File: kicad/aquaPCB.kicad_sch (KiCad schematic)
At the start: 0 parts

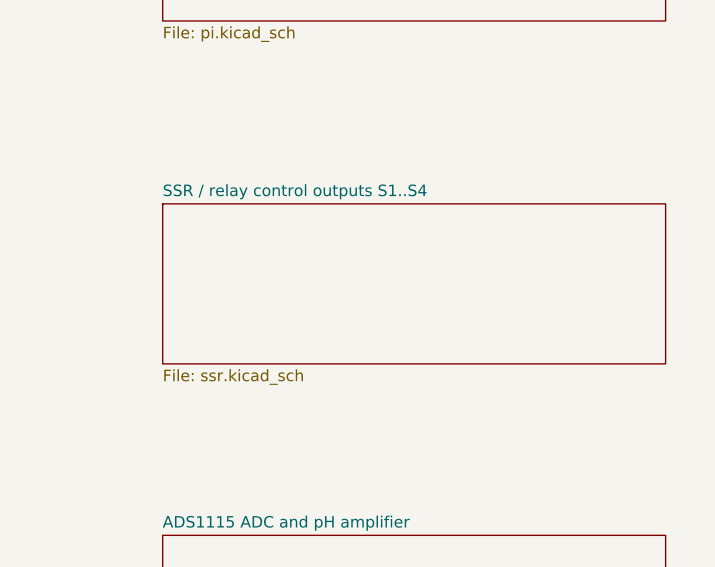
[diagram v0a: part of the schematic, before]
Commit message: kicad: strip obsolete v1 parts for v2 (SSR sheet, IN1..IN4, pH front end)
41 parts, their tracks/vias, pH guard zones, BNC keep-out and port silk removed; freed J2/U5 pins marked no-connect. ERC 0, DRC 0, parity 0; one expected +3V3 ratsnest to J24/JP3/J27/D28 left for the v2 layout.

Co-Authored-By: Claude Opus 5.5 <noreply@anthropic.com>
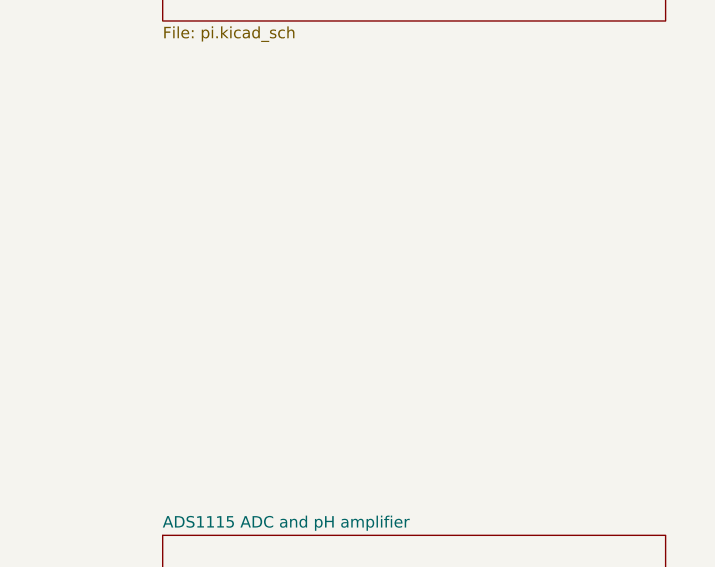
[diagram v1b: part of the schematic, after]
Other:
- removed sheet SSR / relay control outputs S1..S4
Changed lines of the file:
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@@
 			(project "aquaPCB"
 				(path "/80232f81-1179-4777-a7f0-674a974d53cc"
-					(page "6")
+					(page "5")
 				)
 			)
@@
 			(project "aquaPCB"
 				(path "/80232f81-1179-4777-a7f0-674a974d53cc"
-					(page "7")
+					(page "6")
 				)
 			)
@@
 				)
 			)
-		)
-	)
-	(sheet
-		(at 106.68 76.2)
-		(size 55.88 17.78)
-		(exclude_from_sim no)
-		(in_bom yes)
-		(on_board yes)
-		(dnp no)
-		(fields_autoplaced yes)
-		(stroke
-			(width 0.1524)
-			(type solid)
-		)
-		(fill
-			(color 0 0 0 0)
-		)
-		(property "Sheetname" "SSR / relay control outputs S1..S4"
-			(at 106.68 75.4884 0)
-			(show_name no)
-			(do_not_autoplace no)
-			(effects
-				(font
-					(size 1.27 1.27)
-				)
-				(justify left bottom)
-			)
-		)
-		(property "Sheetfile" "ssr.kicad_sch"
-			(at 106.68 94.5684 0)
-			(show_name no)
-			(do_not_autoplace no)
-			(effects
-				(font
-					(size 1.27 1.27)
-				)
-				(justify left top)
-			)
-		)
-		(instances
-			(project "aquaPCB"
-				(path "/80232f81-1179-4777-a7f0-674a974d53cc"
-					(page "5")
-				)
-			)

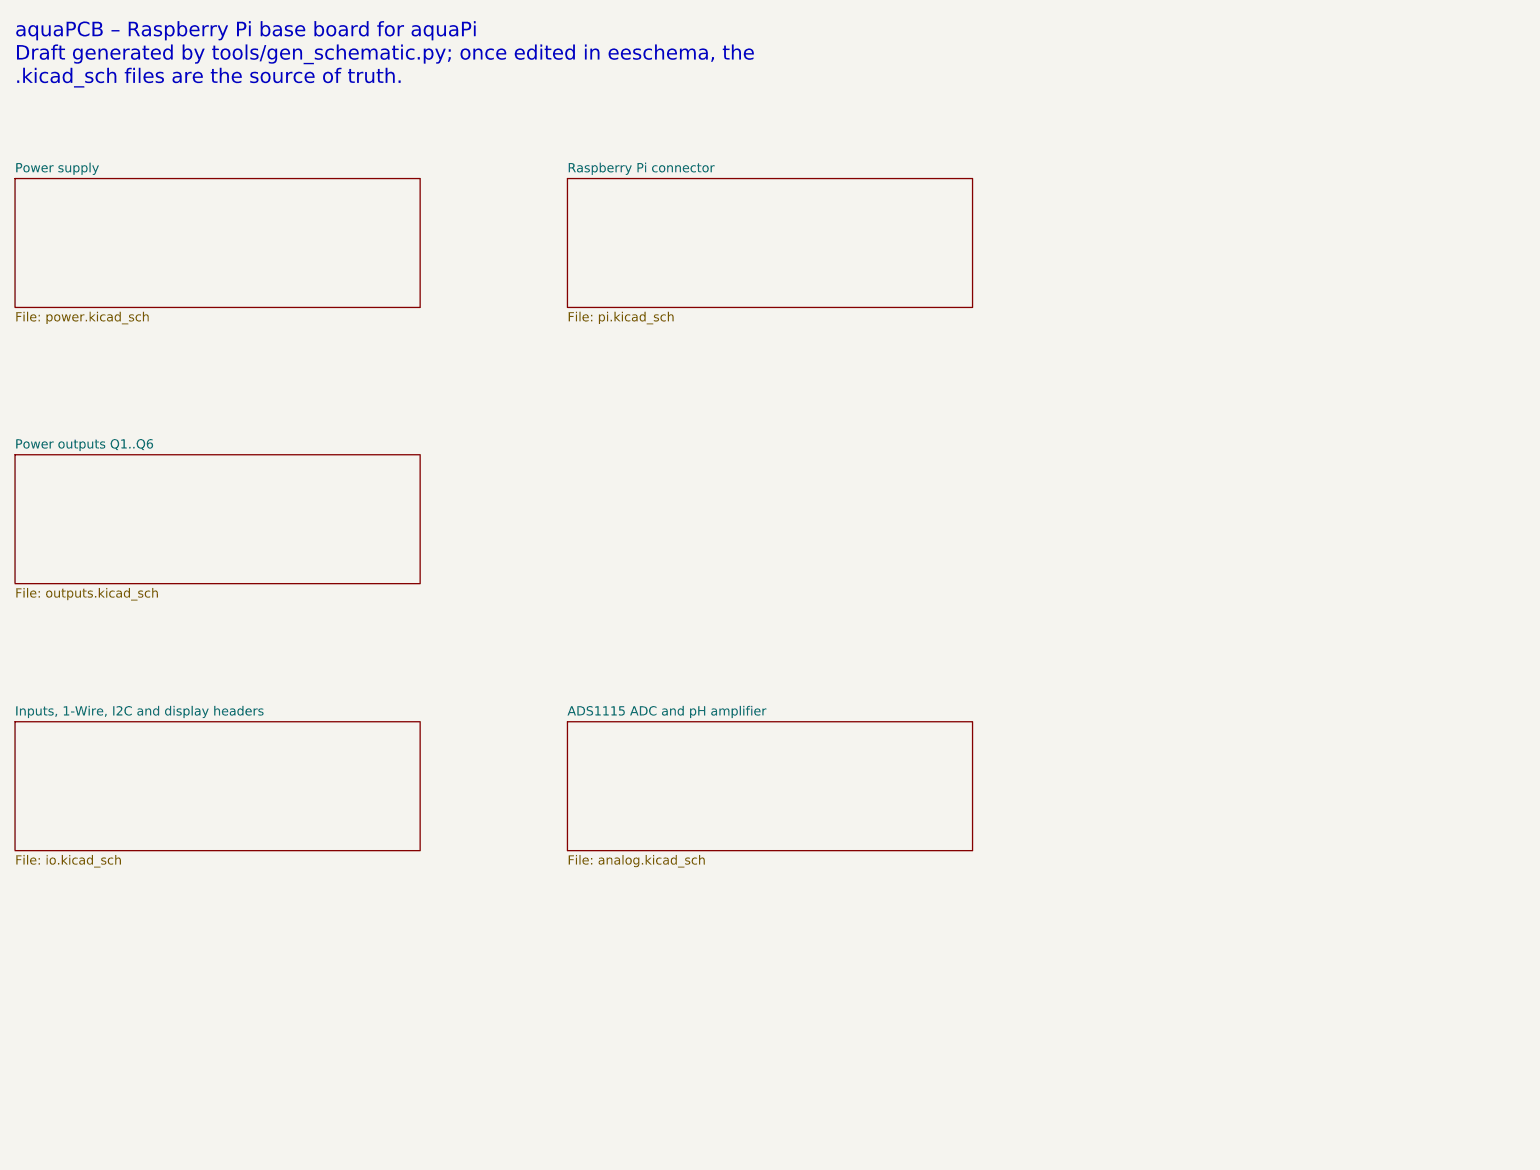
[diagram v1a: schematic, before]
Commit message: kicad: v2 schematic and board update (PCA9685 x2, box-header ports, sensors, analog sockets)
New sheets pwm/powerbar/sensors; Q2/3/5/6 on PCA #1 ch 15-12; sensor GPIOs 5,6,20,21,22,23; 1-Wire +5V_EXT/Data/GND; four identical 0-5 V analog sockets; DC/LED/sensor ports as 2x4 box headers (pin n = Robo-Tank v3 RJ45 pin n). Board: 82 new footprints coarse-placed (56 parked beside the board), ERC 0, DRC copper 0, parity 0. README v2 plan updated.

Co-Authored-By: Claude Opus 5.5 <noreply@anthropic.com>
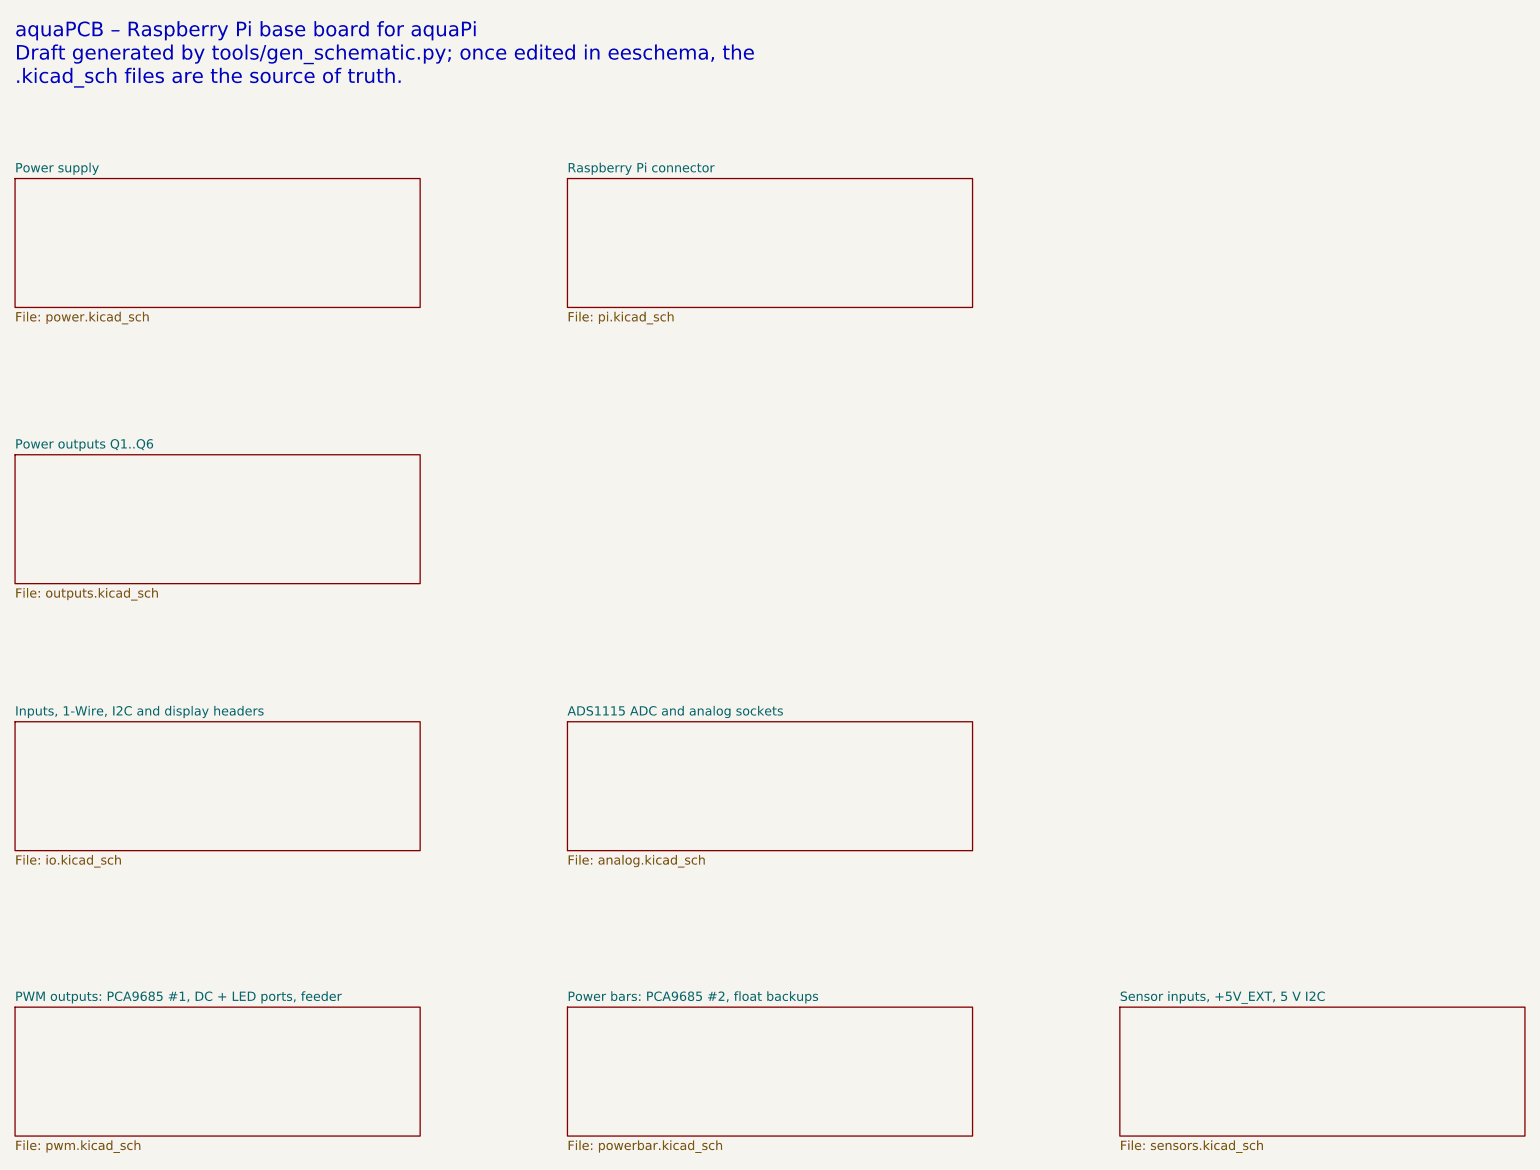
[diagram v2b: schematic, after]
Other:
- sheet ADS1115 ADC and pH amplifier renamed ADS1115 ADC and analog sockets
- added sheet PWM outputs: PCA9685 #1, DC + LED ports, feeder (pwm.kicad_sch)
- added sheet Power bars: PCA9685 #2, float backups (powerbar.kicad_sch)
- added sheet Sensor inputs, +5V_EXT, 5 V I2C (sensors.kicad_sch)
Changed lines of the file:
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@@
 			(color 0 0 0 0)
 		)
-		(property "Sheetname" "ADS1115 ADC and pH amplifier"
+		(property "Sheetname" "ADS1115 ADC and analog sockets"
 			(at 106.68 112.3184 0)
 			(show_name no)
@@
 				)
 			)
+		)
+	)
+	(sheet
+		(at 30.48 152.4)
+		(size 55.88 17.78)
+		(exclude_from_sim no)
+		(in_bom yes)
+		(on_board yes)
+		(dnp no)
+		(fields_autoplaced yes)
+		(stroke
+			(width 0.1524)
+			(type solid)
+		)
+		(fill
+			(color 0 0 0 0)
+		)
+		(property "Sheetname" "PWM outputs: PCA9685 #1, DC + LED ports, feeder"
+			(at 30.48 151.688 0)
+			(show_name no)
+			(do_not_autoplace no)
+			(effects
+				(font
+					(size 1.27 1.27)
+				)
+				(justify left bottom)
+			)
+		)
+		(property "Sheetfile" "pwm.kicad_sch"
+			(at 30.48 170.768 0)
+			(show_name no)
+			(do_not_autoplace no)
+			(effects
+				(font
+					(size 1.27 1.27)
+				)
+				(justify left top)
+			)
+		)
+		(instances
+			(project "aquaPCB"
+				(path "/80232f81-1179-4777-a7f0-674a974d53cc"
+					(page "7")
+				)
+			)
+		)
+	)
+	(sheet
+		(at 106.68 152.4)
+		(size 55.88 17.78)
+		(exclude_from_sim no)
+		(in_bom yes)
+		(on_board yes)
+		(dnp no)
+		(fields_autoplaced yes)
+		(stroke
+			(width 0.1524)
+			(type solid)
+		)
+		(fill
+			(color 0 0 0 0)
+		)
+		(property "Sheetname" "Power bars: PCA9685 #2, float backups"
+			(at 106.68 151.688 0)
+			(show_name no)
+			(do_not_autoplace no)
+			(effects
+				(font
+					(size 1.27 1.27)
+				)
+				(justify left bottom)
+			)
+		)
+		(property "Sheetfile" "powerbar.kicad_sch"
+			(at 106.68 170.768 0)
+			(show_name no)
+			(do_not_autoplace no)
+			(effects
+				(font
+					(size 1.27 1.27)
+				)
+				(justify left top)
+			)
+		)
+		(instances
+			(project "aquaPCB"
+				(path "/80232f81-1179-4777-a7f0-674a974d53cc"
+					(page "8")
+				)
+			)
+		)
+	)
+	(sheet
+		(at 182.88 152.4)
+		(size 55.88 17.78)
+		(exclude_from_sim no)
+		(in_bom yes)
+		(on_board yes)
+		(dnp no)
+		(fields_autoplaced yes)
+		(stroke
+			(width 0.1524)
+			(type solid)
+		)
+		(fill
+			(color 0 0 0 0)
+		)
+		(property "Sheetname" "Sensor inputs, +5V_EXT, 5 V I2C"
+			(at 182.88 151.688 0)
+			(show_name no)
+			(do_not_autoplace no)
+			(effects
+				(font
+					(size 1.27 1.27)
+				)
+				(justify left bottom)
+			)
+		)
+		(property "Sheetfile" "sensors.kicad_sch"
+			(at 182.88 170.768 0)
+			(show_name no)
+			(do_not_autoplace no)
+			(effects
+				(font
+					(size 1.27 1.27)
+				)
+				(justify left top)
+			)
+		)
+		(instances
+			(project "aquaPCB"
+				(path "/80232f81-1179-4777-a7f0-674a974d53cc"
+					(page "9")
+				)
+			)
